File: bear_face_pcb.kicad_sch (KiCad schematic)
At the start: 201 parts, among them J1 USB-C, J2 Conn_02x03_Odd_Even, SW1 RESET, U1 ATmega32U4-AU, U2 SRV05-4, Y1 16MHz

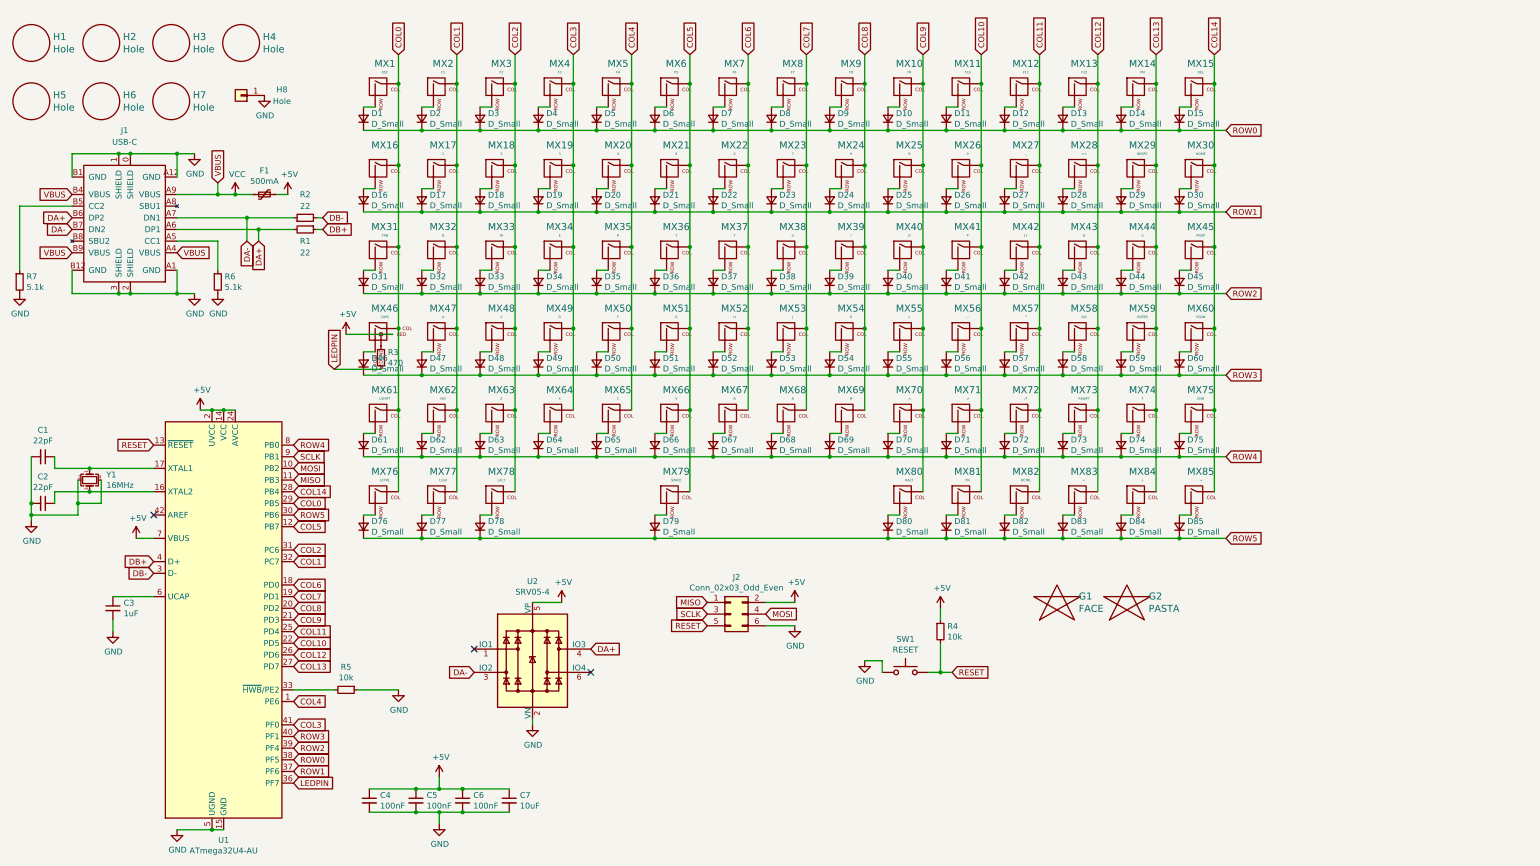
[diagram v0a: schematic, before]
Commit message: initial plate cutout, hole changes * WIP
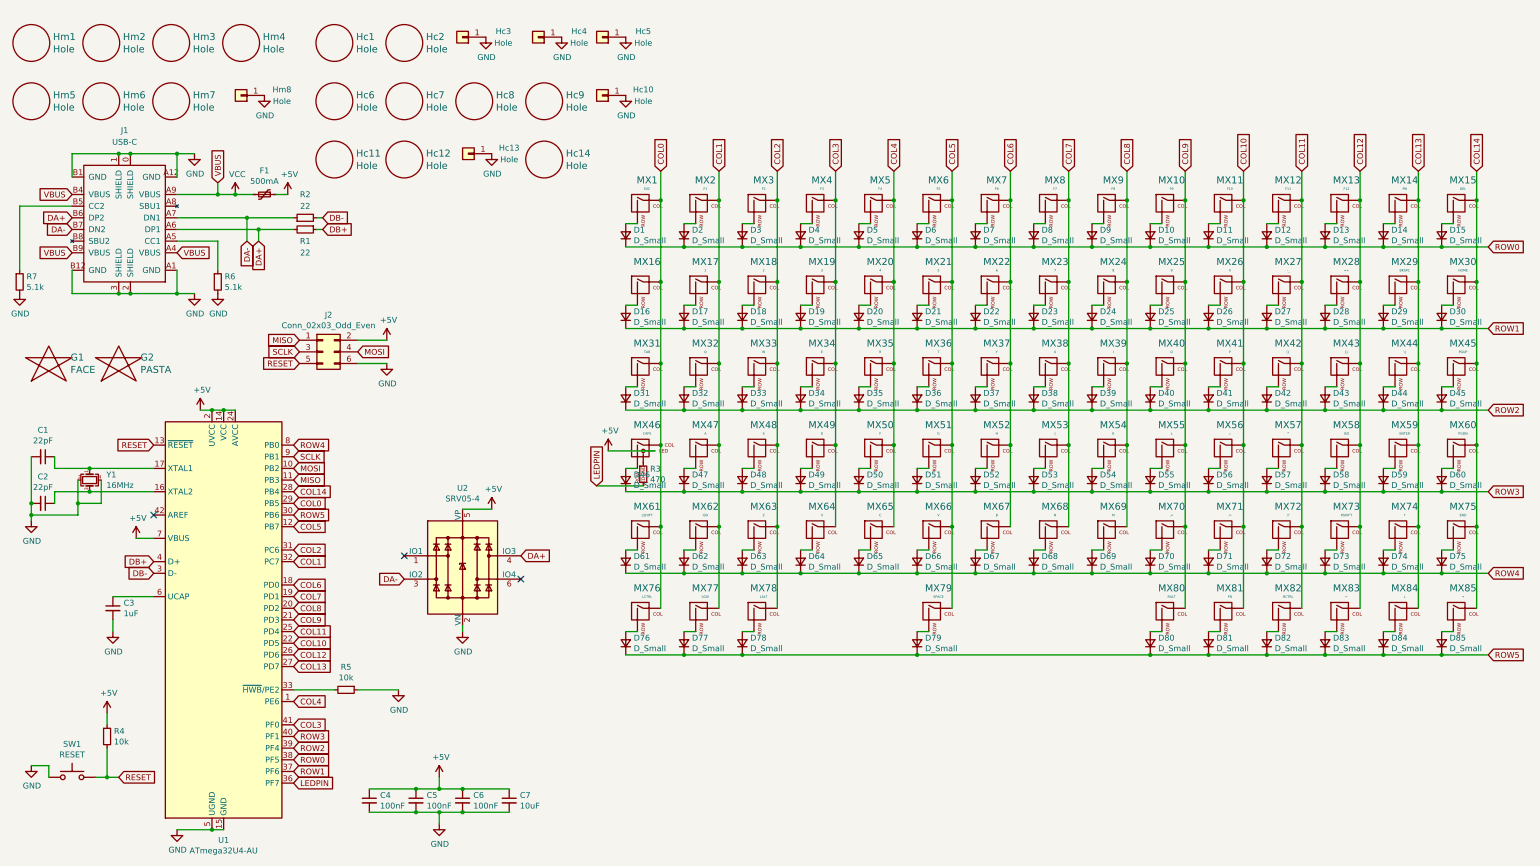
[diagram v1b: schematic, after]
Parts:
- added Hc1, Hc11, Hc12, Hc14, Hc2, Hc6, Hc7, Hc8, Hc9: Hole, bear_face_parts:MountingHole_6mm, symbol keebio:Hole
- added Hc10, Hc13, Hc3, Hc4, Hc5: Hole, MountingHole:MountingHole_2.2mm_M2_Pad, symbol Connector_Generic:Conn_01x01
- renumbered H1 to Hm1, H2 to Hm2, H3 to Hm3, H4 to Hm4, H5 to Hm5, H6 to Hm6, H7 to Hm7, H8 to Hm8
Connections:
- net GND: now also Hc10.1 (Pin_1), Hc13.1 (Pin_1), Hc3.1 (Pin_1), Hc4.1 (Pin_1), Hc5.1 (Pin_1)
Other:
- moved on the sheet: D1, D10, D11, D12, D13, D14, D15, D16, D17, D18, D19, D2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

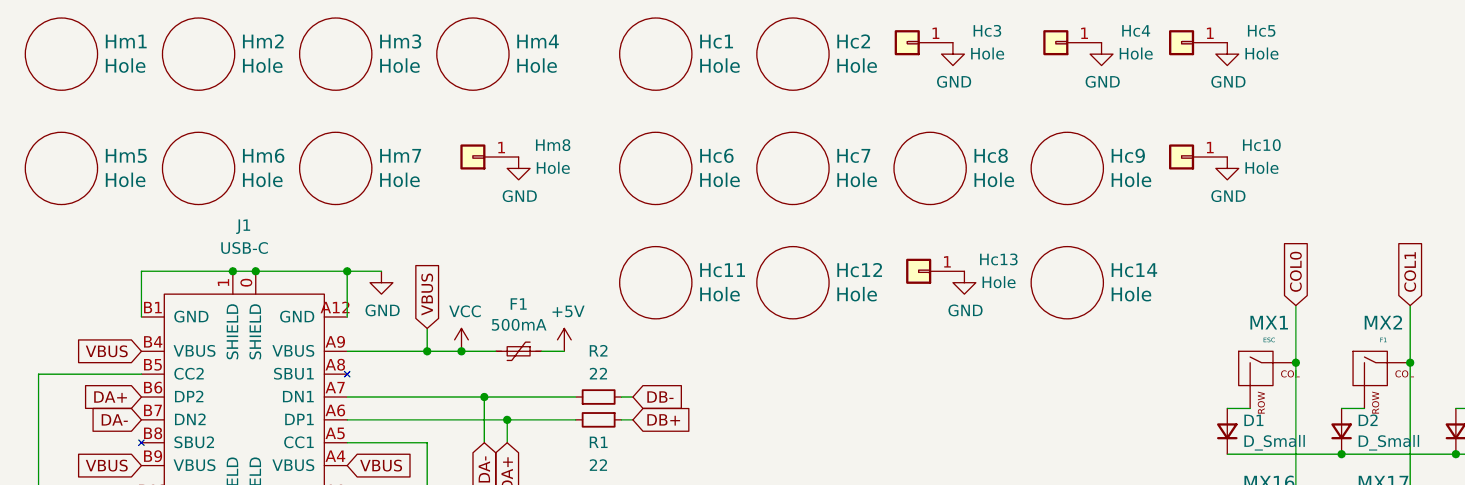
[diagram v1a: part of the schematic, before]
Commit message: moved MCU up to make board smaller * major routing overhaul * stabilized spacebar stab mounts
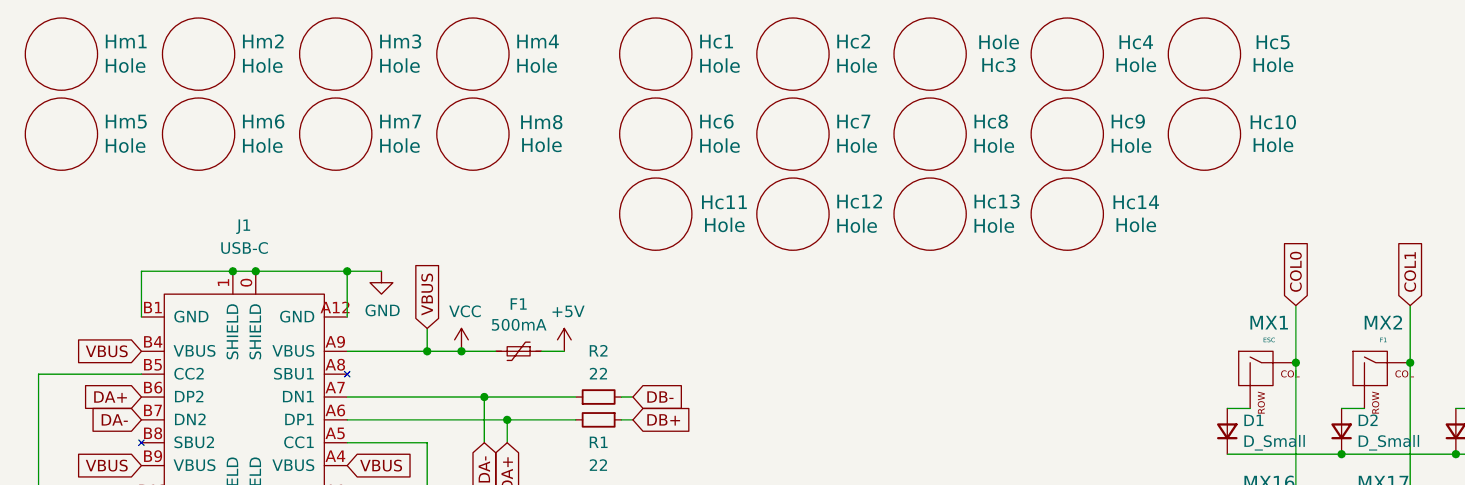
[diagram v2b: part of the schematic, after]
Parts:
- removed Hc14: Hole, bear_face_parts:MountingHole_6mm, symbol keebio:Hole
- added Hc10: Hole, bear_face_parts:MountingHole_6mm, symbol keebio:Hole
- Hc11: renamed from Hc10; footprint MountingHole:MountingHole_2.2mm_M2_Pad -> bear_face_parts:MountingHole_6mm; symbol Connector_Generic:Conn_01x01 -> keebio:Hole
- Hc14: renamed from Hc13; footprint MountingHole:MountingHole_2.2mm_M2_Pad -> bear_face_parts:MountingHole_6mm; symbol Connector_Generic:Conn_01x01 -> keebio:Hole
- Hc3, Hc4, Hc5: footprint MountingHole:MountingHole_2.2mm_M2_Pad -> bear_face_parts:MountingHole_6mm; symbol Connector_Generic:Conn_01x01 -> keebio:Hole
- Hm8: symbol Connector_Generic:Conn_01x01 -> keebio:Hole
- renumbered Hc11 to Hc12, Hc12 to Hc13
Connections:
- net GND: no longer Hc11.1 (Pin_1), Hc14.1 (Pin_1), Hc3.1 (Pin_1), Hc4.1 (Pin_1), Hc5.1 (Pin_1), Hm8.1 (Pin_1)
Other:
- moved on the sheet: Hc12, Hc13, Hc6, Hc7, Hc8, Hc9, Hm5, Hm6, Hm7

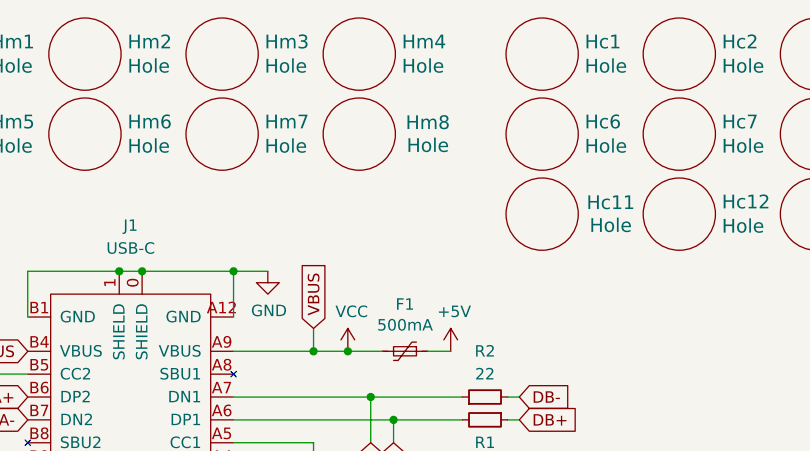
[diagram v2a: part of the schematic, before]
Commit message: minor track, gnd, silk tweaks * technically v3.1c since other 3.1c never printed * will change branch name if protos ok * .gitignore now working
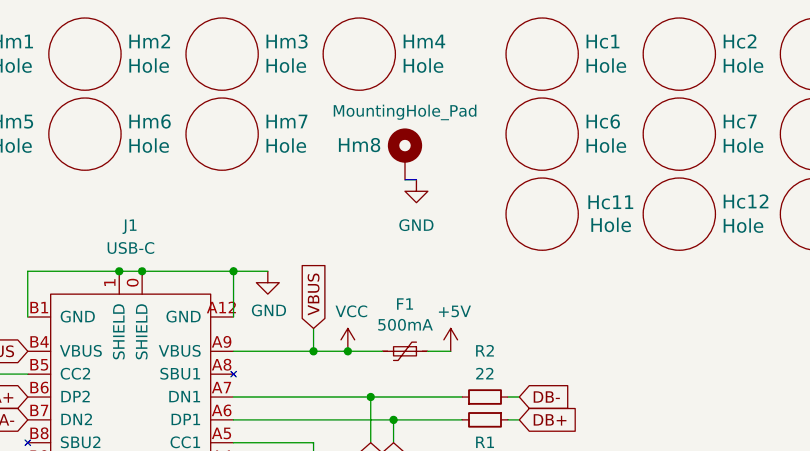
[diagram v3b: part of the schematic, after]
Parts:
- Hm8: value Hole -> MountingHole_Pad; footprint MountingHole:MountingHole_2.2mm_M2_Pad -> bear_face_parts:MountingHole_Header_Pin_Pad; symbol keebio:Hole -> Mechanical:MountingHole_Pad
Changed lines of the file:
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@@
     (stroke (width 0) (type default))
   )
+  (bus (pts (xy 68.58 31.75) (xy 69.85 31.75))
+    (stroke (width 0) (type default))
+  )
   (wire (pts (xy 223.52 110.49) (xy 226.06 110.49))
     (stroke (width 0) (type default))
@@
     )
   )
-  (symbol (lib_id "keebio:Hole") (at 63.5 26.67 180) (unit 1)
+  (symbol (lib_id "Mechanical:MountingHole_Pad") (at 68.58 29.21 0) (unit 1)
     (in_bom yes) (on_board yes) (dnp no)
-    (property "Reference" "Hm8" (at 71.12 25.4 0)
+    (property "Reference" "Hm8" (at 63.5 27.94 0)
       (effects (font (size 1.524 1.524)))
     )
-    (property "Value" "Hole" (at 71.12 27.94 0)
-      (effects (font (size 1.524 1.524)))
+    (property "Value" "MountingHole_Pad" (at 68.58 24.13 0)
+      (effects (font (size 1.27 1.27)))
     )
-    (property "Footprint" "MountingHole:MountingHole_2.2mm_M2_Pad" (at 63.5 26.67 0)
-      (effects (font (size 1.524 1.524)) hide)
+    (property "Footprint" "bear_face_parts:MountingHole_Header_Pin_Pad" (at 68.58 29.21 0)
+      (effects (font (size 1.27 1.27)) hide)
     )
-    (property "Datasheet" "~" (at 63.5 26.67 0)
-      (effects (font (size 1.524 1.524)) hide)
+    (property "Datasheet" "~" (at 68.58 29.21 0)
+      (effects (font (size 1.27 1.27)) hide)
     )
+    (pin "1")
     (instances
       (project "bear_face_pcb"
@@
         )
       )
+    )
+  )
+  (symbol (lib_id "power:GND") (at 69.85 31.75 0) (unit 1)
+    (in_bom yes) (on_board yes) (dnp no) (fields_autoplaced)
+    (property "Reference" "#PWR01" (at 69.85 38.1 0)
+      (effects (font (size 1.27 1.27)) hide)
+    )
+    (property "Value" "GND" (at 69.85 36.83 0)
+      (effects (font (size 1.27 1.27)))
+    )
+    (property "Footprint" "" (at 69.85 31.75 0)
+      (effects (font (size 1.27 1.27)) hide)
+    )
+    (property "Datasheet" "" (at 69.85 31.75 0)
+      (effects (font (size 1.27 1.27)) hide)
+    )
+    (pin "1")
+    (instances
+      (project "bear_face_pcb"
+        (path "/cabe0d99-90c0-4856-a4d9-0ecf66edd542"
+          (reference "#PWR01") (unit 1)
+        )
+      )

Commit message: updated plugin attrs, gerbers
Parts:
- Hc1, Hc10, Hc11, Hc12, Hc13, Hc14, Hc2, Hc3, Hc4, Hc5, Hc6, Hc7, Hc8, Hc9, Hm1, Hm2, Hm3, Hm4, Hm5, Hm6, Hm7, Hm8: now not fitted; now left out of the parts list
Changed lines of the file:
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@@
   )
   (symbol (lib_id "keebio:Hole") (at 33.02 17.78 0) (unit 1)
-    (in_bom yes) (on_board yes) (dnp no)
+    (in_bom no) (on_board yes) (dnp yes)
     (property "Reference" "Hm2" (at 37.7444 16.4338 0)
       (effects (font (size 1.524 1.524)) (justify left))
@@
   )
   (symbol (lib_id "keebio:Hole") (at 48.26 17.78 0) (unit 1)
-    (in_bom yes) (on_board yes) (dnp no)
+    (in_bom no) (on_board yes) (dnp yes)
     (property "Reference" "Hm3" (at 52.9844 16.4338 0)
       (effects (font (size 1.524 1.524)) (justify left))
@@
   )
   (symbol (lib_id "keebio:Hole") (at 48.26 26.67 0) (unit 1)
-    (in_bom yes) (on_board yes) (dnp no)
+    (in_bom no) (on_board yes) (dnp yes)
     (property "Reference" "Hm7" (at 52.9844 25.3238 0)
       (effects (font (size 1.524 1.524)) (justify left))
@@
   )
   (symbol (lib_id "keebio:Hole") (at 17.78 17.78 0) (unit 1)
-    (in_bom yes) (on_board yes) (dnp no)
+    (in_bom no) (on_board yes) (dnp yes)
     (property "Reference" "Hm1" (at 22.5044 16.4338 0)
       (effects (font (size 1.524 1.524)) (justify left))
@@
   )
   (symbol (lib_id "keebio:Hole") (at 17.78 26.67 0) (unit 1)
-    (in_bom yes) (on_board yes) (dnp no)
+    (in_bom no) (on_board yes) (dnp yes)
     (property "Reference" "Hm5" (at 22.5044 25.3238 0)
       (effects (font (size 1.524 1.524)) (justify left))
@@
   )
   (symbol (lib_id "keebio:Hole") (at 33.02 26.67 0) (unit 1)
-    (in_bom yes) (on_board yes) (dnp no)
+    (in_bom no) (on_board yes) (dnp yes)
     (property "Reference" "Hm6" (at 37.7444 25.3238 0)
       (effects (font (size 1.524 1.524)) (justify left))
@@
   )
   (symbol (lib_id "keebio:Hole") (at 63.5 17.78 0) (unit 1)
-    (in_bom yes) (on_board yes) (dnp no)
+    (in_bom no) (on_board yes) (dnp yes)
     (property "Reference" "Hm4" (at 68.2244 16.4338 0)
       (effects (font (size 1.524 1.524)) (justify left))
@@
   )
   (symbol (lib_id "Mechanical:MountingHole_Pad") (at 68.58 29.21 0) (unit 1)
-    (in_bom yes) (on_board yes) (dnp no)
+    (in_bom no) (on_board yes) (dnp yes)
     (property "Reference" "Hm8" (at 63.5 27.94 0)
       (effects (font (size 1.524 1.524)))
@@
   )
   (symbol (lib_id "keebio:Hole") (at 144.78 17.78 180) (unit 1)
-    (in_bom yes) (on_board yes) (dnp no)
+    (in_bom no) (on_board yes) (dnp yes)
     (property "Reference" "Hc5" (at 152.4 16.51 0)
       (effects (font (size 1.524 1.524)))
@@
   )
   (symbol (lib_id "keebio:Hole") (at 83.82 17.78 0) (unit 1)
-    (in_bom yes) (on_board yes) (dnp no)
+    (in_bom no) (on_board yes) (dnp yes)
     (property "Reference" "Hc1" (at 88.5444 16.4338 0)
       (effects (font (size 1.524 1.524)) (justify left))
@@
   )
   (symbol (lib_id "keebio:Hole") (at 114.3 17.78 0) (unit 1)
-    (in_bom yes) (on_board yes) (dnp no)
+    (in_bom no) (on_board yes) (dnp yes)
     (property "Reference" "Hc3" (at 121.92 19.05 0)
       (effects (font (size 1.524 1.524)))
@@
   )
   (symbol (lib_id "keebio:Hole") (at 83.82 35.56 180) (unit 1)
-    (in_bom yes) (on_board yes) (dnp no)
+    (in_bom no) (on_board yes) (dnp yes)
     (property "Reference" "Hc11" (at 91.44 34.29 0)
       (effects (font (size 1.524 1.524)))
@@
   )
   (symbol (lib_id "keebio:Hole") (at 114.3 35.56 0) (unit 1)
-    (in_bom yes) (on_board yes) (dnp no)
+    (in_bom no) (on_board yes) (dnp yes)
     (property "Reference" "Hc13" (at 119.0244 34.2138 0)
       (effects (font (size 1.524 1.524)) (justify left))
@@
   )
   (symbol (lib_id "keebio:Hole") (at 99.06 35.56 0) (unit 1)
-    (in_bom yes) (on_board yes) (dnp no)
+    (in_bom no) (on_board yes) (dnp yes)
     (property "Reference" "Hc12" (at 103.7844 34.2138 0)
       (effects (font (size 1.524 1.524)) (justify left))
@@
   )
   (symbol (lib_id "keebio:Hole") (at 83.82 26.67 0) (unit 1)
-    (in_bom yes) (on_board yes) (dnp no)
+    (in_bom no) (on_board yes) (dnp yes)
     (property "Reference" "Hc6" (at 88.5444 25.3238 0)
       (effects (font (size 1.524 1.524)) (justify left))
@@
   )
   (symbol (lib_id "keebio:Hole") (at 144.78 26.67 180) (unit 1)
-    (in_bom yes) (on_board yes) (dnp no)
+    (in_bom no) (on_board yes) (dnp yes)
     (property "Reference" "Hc10" (at 152.4 25.4 0)
       (effects (font (size 1.524 1.524)))
@@
   )
   (symbol (lib_id "keebio:Hole") (at 114.3 26.67 0) (unit 1)
-    (in_bom yes) (on_board yes) (dnp no)
+    (in_bom no) (on_board yes) (dnp yes)
     (property "Reference" "Hc8" (at 119.0244 25.3238 0)
       (effects (font (size 1.524 1.524)) (justify left))
@@
   )
   (symbol (lib_id "keebio:Hole") (at 129.54 26.67 0) (unit 1)
-    (in_bom yes) (on_board yes) (dnp no)
+    (in_bom no) (on_board yes) (dnp yes)
     (property "Reference" "Hc9" (at 134.2644 25.3238 0)
       (effects (font (size 1.524 1.524)) (justify left))
@@
   )
   (symbol (lib_id "keebio:Hole") (at 99.06 26.67 0) (unit 1)
-    (in_bom yes) (on_board yes) (dnp no)
+    (in_bom no) (on_board yes) (dnp yes)
     (property "Reference" "Hc7" (at 103.7844 25.3238 0)
       (effects (font (size 1.524 1.524)) (justify left))
@@
   )
   (symbol (lib_id "keebio:Hole") (at 129.54 35.56 180) (unit 1)
-    (in_bom yes) (on_board yes) (dnp no)
+    (in_bom no) (on_board yes) (dnp yes)
     (property "Reference" "Hc14" (at 137.16 34.29 0)
       (effects (font (size 1.524 1.524)))
@@
   )
   (symbol (lib_id "keebio:Hole") (at 99.06 17.78 0) (unit 1)
-    (in_bom yes) (on_board yes) (dnp no)
+    (in_bom no) (on_board yes) (dnp yes)
     (property "Reference" "Hc2" (at 103.7844 16.4338 0)
       (effects (font (size 1.524 1.524)) (justify left))
@@
   )
   (symbol (lib_id "keebio:Hole") (at 129.54 17.78 180) (unit 1)
-    (in_bom yes) (on_board yes) (dnp no)
+    (in_bom no) (on_board yes) (dnp yes)
     (property "Reference" "Hc4" (at 137.16 16.51 0)
       (effects (font (size 1.524 1.524)))

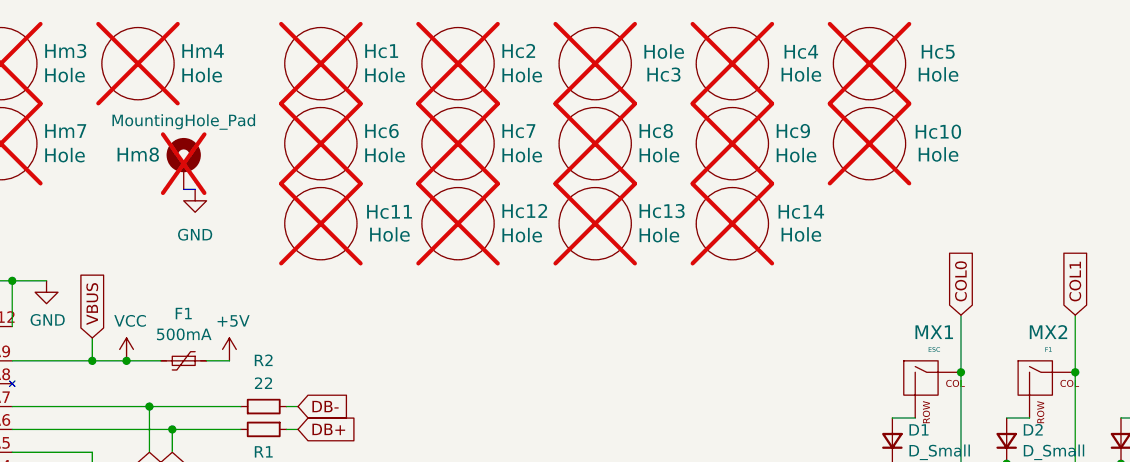
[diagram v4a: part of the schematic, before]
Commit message: rounded stab area pcb, new gerbers, minor silks tweaks
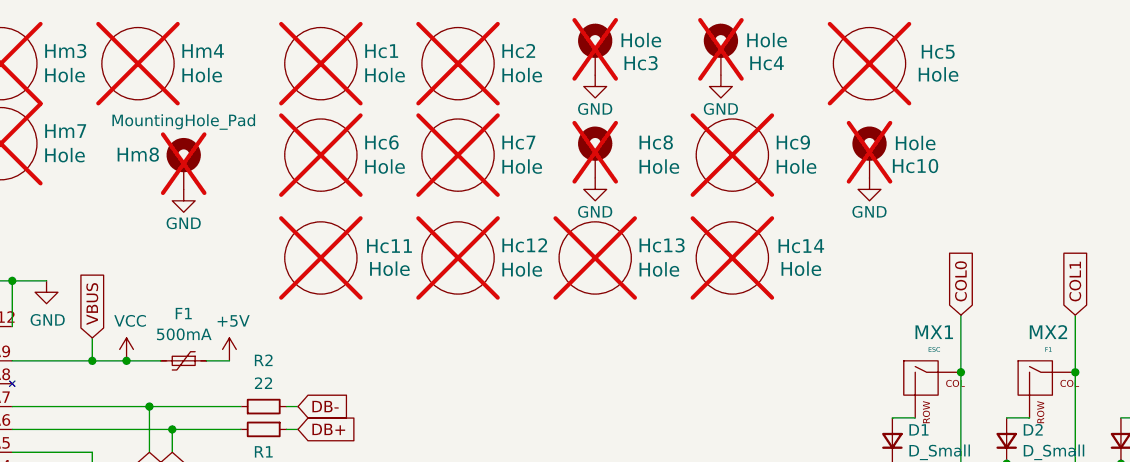
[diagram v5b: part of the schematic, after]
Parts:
- Hc10, Hc3, Hc4, Hc8: footprint bear_face_parts:MountingHole_6mm -> MountingHole:MountingHole_2.2mm_M2_Pad; symbol keebio:Hole -> Mechanical:MountingHole_Pad; now in the parts list
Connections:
- net GND: now also Hc10.1, Hc3.1, Hc4.1, Hc8.1, Hm8.1
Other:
- moved on the sheet: Hc11, Hc12, Hc13, Hc14, Hc6, Hc7, Hc9
